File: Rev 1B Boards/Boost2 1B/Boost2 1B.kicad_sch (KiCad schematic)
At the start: 2 parts, among them J27 Banana 2P, J28 Banana 2P

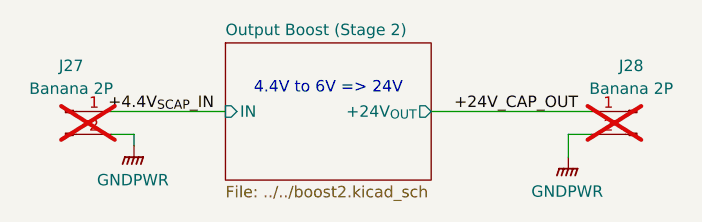
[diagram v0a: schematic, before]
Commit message: Replace most banana jacks with XT connectors
+ update library
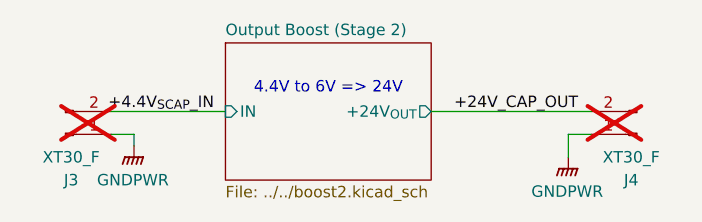
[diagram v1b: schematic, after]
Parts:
- removed J27, J28: Banana 2P, Connector:Banana_Jack_2Pin, symbol Connector:Conn_01x02_Pin
- added J3, J4: XT30_F, Connector_AMASS:AMASS_XT30U-F_1x02_P5.0mm_Vertical, symbol Connector:Conn_01x02_Pin
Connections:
- net +24V_CAP_OUT: now also J4.2 (Pin_2)
- net +4.4V_{SCAP}_IN: now also J3.2 (Pin_2)
- net GNDPWR: now also J3.1 (Pin_1), J4.1 (Pin_1)
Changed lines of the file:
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@@
+	)
+	(symbol
+		(lib_id "Connector:Conn_01x02_Pin")
+		(at 66.04 63.5 0)
+		(mirror x)
+		(unit 1)
+		(exclude_from_sim no)
+		(in_bom yes)
+		(on_board yes)
+		(dnp yes)
+		(property "Reference" "J3"
+			(at 66.675 68.58 0)
+			(effects
+				(font
+					(size 1.27 1.27)
+				)
+			)
+		)
+		(property "Value" "XT30_F"
+			(at 66.675 66.04 0)
+			(effects
+				(font
+					(size 1.27 1.27)
+				)
+			)
+		)
+		(property "Footprint" "Connector_AMASS:AMASS_XT30U-F_1x02_P5.0mm_Vertical"
+			(at 66.04 63.5 0)
+			(effects
+				(font
+					(size 1.27 1.27)
+				)
+				(hide yes)
+			)
+		)
+		(property "Datasheet" "~"
+			(at 66.04 63.5 0)
+			(effects
+				(font
+					(size 1.27 1.27)
+				)
+				(hide yes)
+			)
+		)
+		(property "Description" "Generic connector, single row, 01x02, script generated"
+			(at 66.04 63.5 0)
+			(effects
+				(font
+					(size 1.27 1.27)
+				)
+				(hide yes)
+			)
+		)
+		(property "Sim.Device" ""
+			(at 66.04 63.5 0)
+			(effects
+				(font
+					(size 1.27 1.27)
+				)
+			)
+		)
+		(property "Sim.Pins" ""
+			(at 66.04 63.5 0)
+			(effects
+				(font
+					(size 1.27 1.27)
+				)
+			)
+		)
+		(property "Sim.Type" ""
+			(at 66.04 63.5 0)
+			(effects
+				(font
+					(size 1.27 1.27)
+				)
+			)
+		)
+		(property "Height" ""
+			(at 66.04 63.5 0)
+			(effects
+				(font
+					(size 1.27 1.27)
+				)
+			)
+		)
+		(property "Manufacturer_Name" ""
+			(at 66.04 63.5 0)
+			(effects
+				(font
+					(size 1.27 1.27)
+				)
+			)
+		)
+		(property "Manufacturer_Part_Number" ""
+			(at 66.04 63.5 0)
+			(effects
+				(font
+					(size 1.27 1.27)
+				)
+			)
+		)
+		(property "Mouser Price/Stock" ""
+			(at 66.04 63.5 0)
+			(effects
+				(font
+					(size 1.27 1.27)
+				)
+			)
+		)
+		(pin "1"
+		)
+		(pin "2"
+		)
+		(instances
+			(project "Boost2 1B"
+				(path "/12d7d405-80bc-44f7-b268-462602cf0149"
+					(reference "J3")
+					(unit 1)
+				)
+			)
+		)
 	)
 	(symbol
@@
 	(symbol
 		(lib_id "Connector:Conn_01x02_Pin")
-		(at 66.04 60.96 0)
+		(at 129.54 63.5 180)
 		(unit 1)
 		(exclude_from_sim no)
@@
 		(on_board yes)
 		(dnp yes)
-		(property "Reference" "J27"
-			(at 66.675 55.88 0)
-			(effects
-				(font
-					(size 1.27 1.27)
-				)
-			)
-		)
-		(property "Value" "Banana 2P"
-			(at 66.675 58.42 0)
-			(effects
-				(font
-					(size 1.27 1.27)
-				)
-			)
-		)
-		(property "Footprint" "Connector:Banana_Jack_2Pin"
-			(at 66.04 60.96 0)
+		(property "Reference" "J4"
+			(at 128.905 68.58 0)
+			(effects
+				(font
+					(size 1.27 1.27)
+				)
+			)
+		)
+		(property "Value" "XT30_F"
+			(at 128.905 66.04 0)
+			(effects
+				(font
+					(size 1.27 1.27)
+				)
+			)
+		)
+		(property "Footprint" "Connector_AMASS:AMASS_XT30U-F_1x02_P5.0mm_Vertical"
+			(at 129.54 63.5 0)
 			(effects
 				(font
@@
 		)
 		(property "Datasheet" "~"
-			(at 66.04 60.96 0)
+			(at 129.54 63.5 0)
 			(effects
 				(font
@@
 		)
 		(property "Description" "Generic connector, single row, 01x02, script generated"
-			(at 66.04 60.96 0)
+			(at 129.54 63.5 0)
 			(effects
 				(font
@@
 		)
 		(property "Sim.Device" ""
-			(at 66.04 60.96 0)
+			(at 129.54 63.5 0)
 			(effects
 				(font
@@
 		)
 		(property "Sim.Pins" ""
-			(at 66.04 60.96 0)
+			(at 129.54 63.5 0)
 			(effects
 				(font
@@
 		)
 		(property "Sim.Type" ""
-			(at 66.04 60.96 0)
+			(at 129.54 63.5 0)
 			(effects
 				(font
@@
 		)
 		(property "Height" ""
-			(at 66.04 60.96 0)
+			(at 129.54 63.5 0)
 			(effects
 				(font
@@
 		)
 		(property "Manufacturer_Name" ""
-			(at 66.04 60.96 0)
+			(at 129.54 63.5 0)
 			(effects
 				(font
@@
 		)
 		(property "Manufacturer_Part_Number" ""
-			(at 66.04 60.96 0)
+			(at 129.54 63.5 0)
 			(effects
 				(font
@@
 		)
 		(property "Mouser Price/Stock" ""
-			(at 66.04 60.96 0)
+			(at 129.54 63.5 0)
 			(effects
 				(font
@@
 			(project "Boost2 1B"
 				(path "/12d7d405-80bc-44f7-b268-462602cf0149"
-					(reference "J27")
+					(reference "J4")
 					(unit 1)
 				)
@@
 					(unit 1)
 				)
-			)
-		)
-	)
-	(symbol
-		(lib_id "Connector:Conn_01x02_Pin")
-		(at 129.54 60.96 0)
-		(mirror y)
-		(unit 1)
-		(exclude_from_sim no)
-		(in_bom yes)
-		(on_board yes)
-		(dnp yes)
-		(fields_autoplaced yes)
-		(property "Reference" "J28"
-			(at 128.905 55.88 0)
-			(effects
-				(font
-					(size 1.27 1.27)
-				)
-			)
-		)
-		(property "Value" "Banana 2P"
-			(at 128.905 58.42 0)
-			(effects
-				(font
-					(size 1.27 1.27)
-				)
-			)
-		)
-		(property "Footprint" "Connector:Banana_Jack_2Pin"
-			(at 129.54 60.96 0)
-			(effects
-				(font
-					(size 1.27 1.27)
-				)
-				(hide yes)
-			)
-		)
-		(property "Datasheet" "~"
-			(at 129.54 60.96 0)
-			(effects
-				(font
-					(size 1.27 1.27)
-				)
-				(hide yes)
-			)
-		)
-		(property "Description" "Generic connector, single row, 01x02, script generated"
-			(at 129.54 60.96 0)
-			(effects
-				(font
-					(size 1.27 1.27)
-				)
-				(hide yes)
-			)
-		)
-		(property "Sim.Device" ""
-			(at 129.54 60.96 0)
-			(effects
-				(font
-					(size 1.27 1.27)
-				)
-			)
-		)
-		(property "Sim.Pins" ""
-			(at 129.54 60.96 0)
-			(effects
-				(font
-					(size 1.27 1.27)
-				)
-			)
-		)
-		(property "Sim.Type" ""
-			(at 129.54 60.96 0)
-			(effects
-				(font
-					(size 1.27 1.27)
-				)
-			)
-		)
-		(property "Height" ""
-			(at 129.54 60.96 0)
-			(effects
-				(font
-					(size 1.27 1.27)
-				)
-			)
-		)
-		(property "Manufacturer_Name" ""
-			(at 129.54 60.96 0)
-			(effects
-				(font
-					(size 1.27 1.27)
-				)
-			)
-		)
-		(property "Manufacturer_Part_Number" ""
-			(at 129.54 60.96 0)
-			(effects
-				(font
-					(size 1.27 1.27)
-				)
-			)
-		)
-		(property "Mouser Price/Stock" ""
-			(at 129.54 60.96 0)
-			(effects
-				(font
-					(size 1.27 1.27)
-				)
-			)
-		)
-		(pin "1"
-		)
-		(pin "2"
-		)
-		(instances
-			(project "Boost2 1B"
-				(path "/12d7d405-80bc-44f7-b268-462602cf0149"
-					(reference "J28")
-					(unit 1)
-				)
